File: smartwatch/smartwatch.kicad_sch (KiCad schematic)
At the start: 33 parts, among them J1 BAT_CON, J2 DC_CON, J3 PROG_INT, J4 Screen, J5 Touch, J6 Power, J8 SD Card, SW1 SW_Push, U1 ESP32-WROVER-E, U2 MCP73831-5-OT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

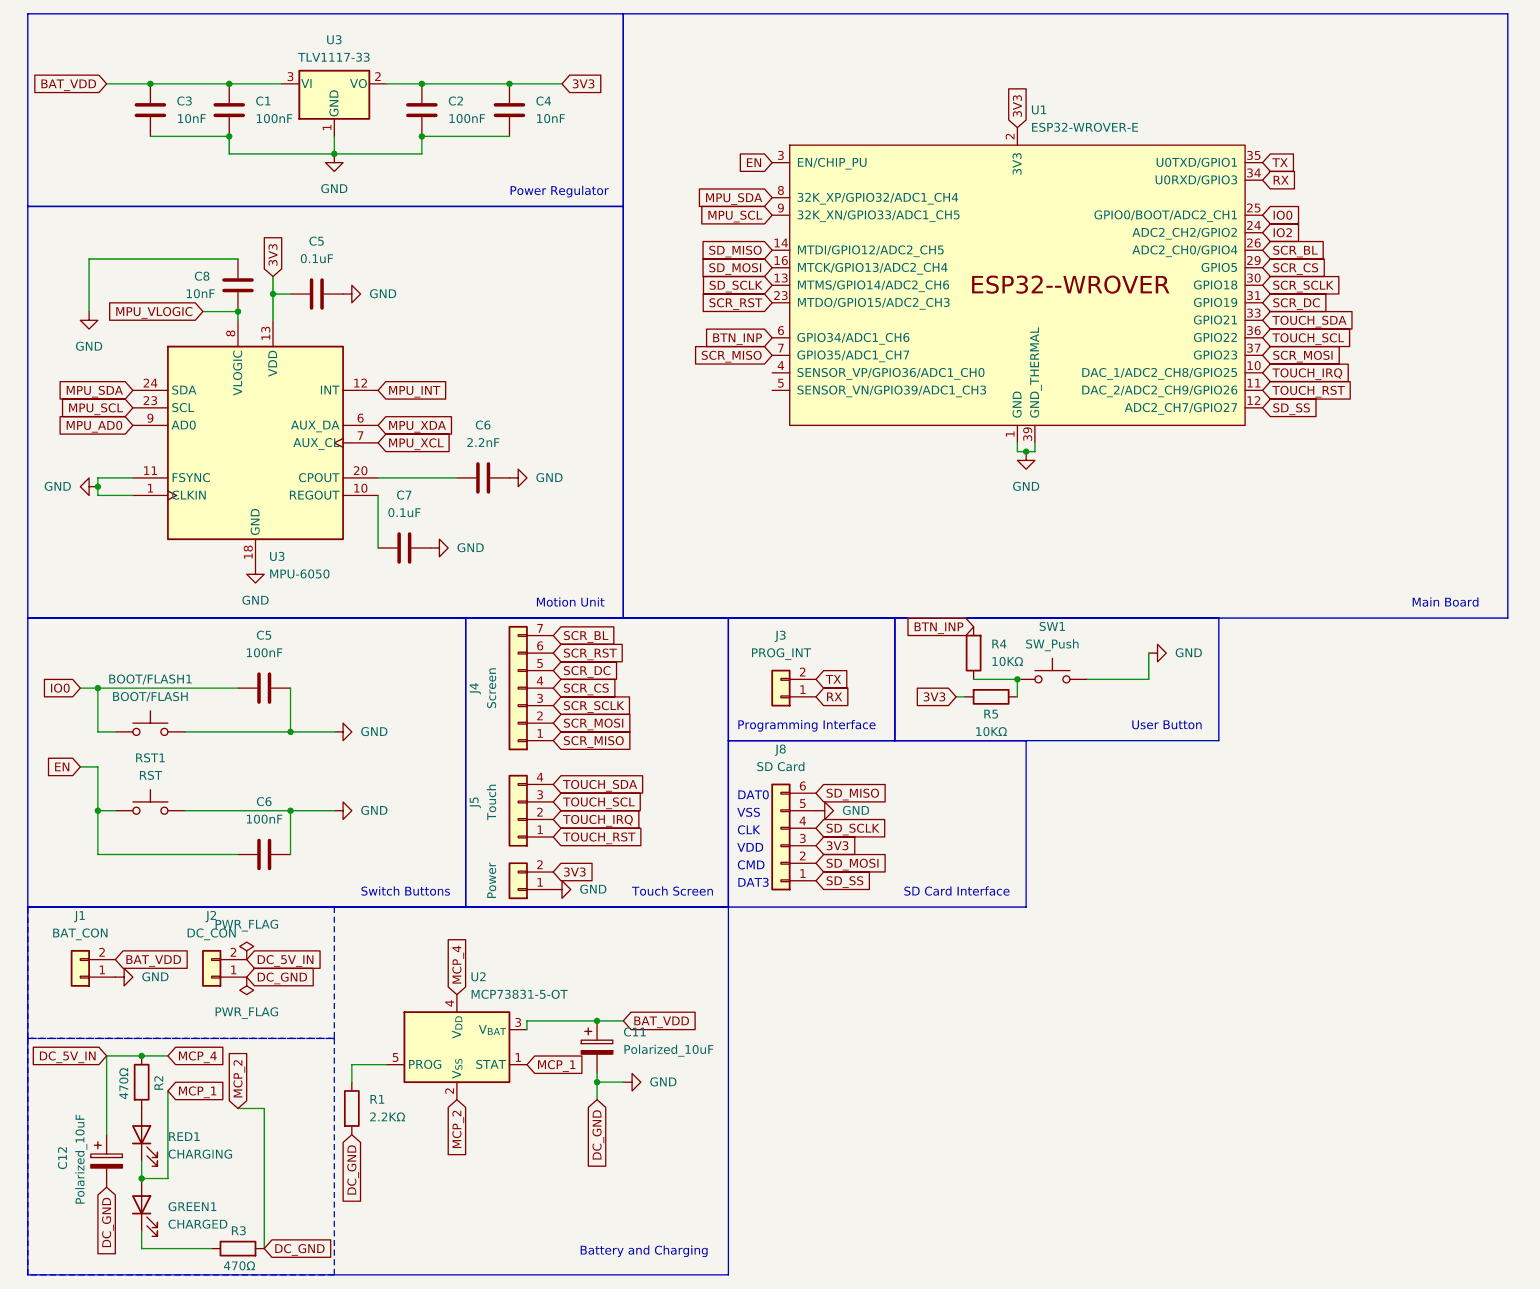
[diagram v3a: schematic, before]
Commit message: fully redesigned board - ground and power planes :)
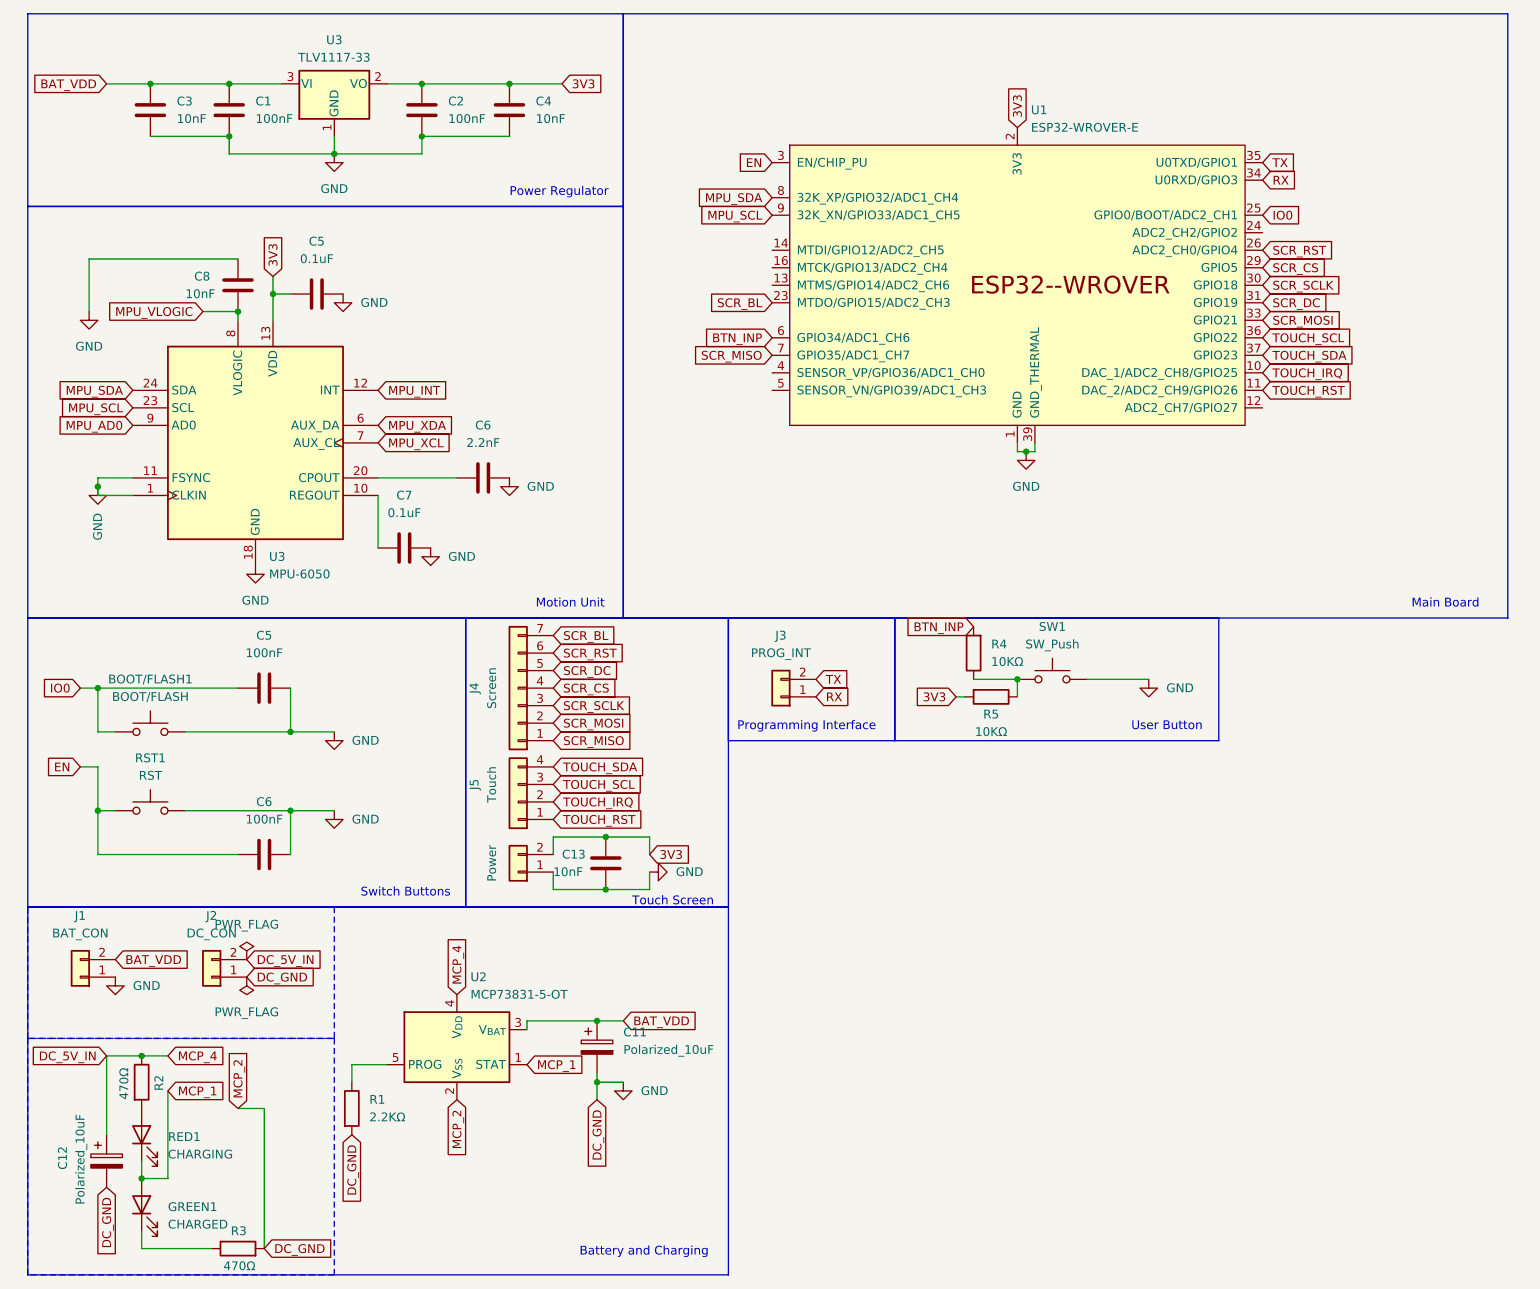
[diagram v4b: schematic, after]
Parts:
- removed J8: SD Card, Connector_Wire_SMD:Wire_Pad_1x06, symbol Connector_Generic:Conn_01x06
- added C13: 10nF, Capacitor_SMD:C_0805_2012Metric_Pad1.18x1.45mm_HandSolder, symbol Device:C
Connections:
- net 3V3: now also C13.2
- net GND: now also C13.1
- net SCR_BL: now also U1.23 (MTDO/GPIO15/ADC2_CH3); no longer U1.26 (ADC2_CH0/GPIO4)
- net SCR_MOSI: now also U1.33 (GPIO21); no longer U1.37 (GPIO23)
- net SCR_RST: now also U1.26 (ADC2_CH0/GPIO4); no longer U1.23 (MTDO/GPIO15/ADC2_CH3)
- net TOUCH_SDA: now also U1.37 (GPIO23); no longer U1.33 (GPIO21)
- net IO2: no longer names the net of U1.24 (ADC2_CH2/GPIO2)
- net SD_MISO: no longer names the net of U1.14 (MTDI/GPIO12/ADC2_CH5)
- net SD_MOSI: no longer names the net of U1.16 (MTCK/GPIO13/ADC2_CH4)
- net SD_SCLK: no longer names the net of U1.13 (MTMS/GPIO14/ADC2_CH6)
- net SD_SS: no longer names the net of U1.12 (ADC2_CH7/GPIO27)
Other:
- note removed: "CLK"
- note removed: "CMD"
- note removed: "DAT0"
- note removed: "DAT3"
- note removed: "SD Card Interface"
- note removed: "VDD"
- note removed: "VSS"
- moved on the sheet: J5

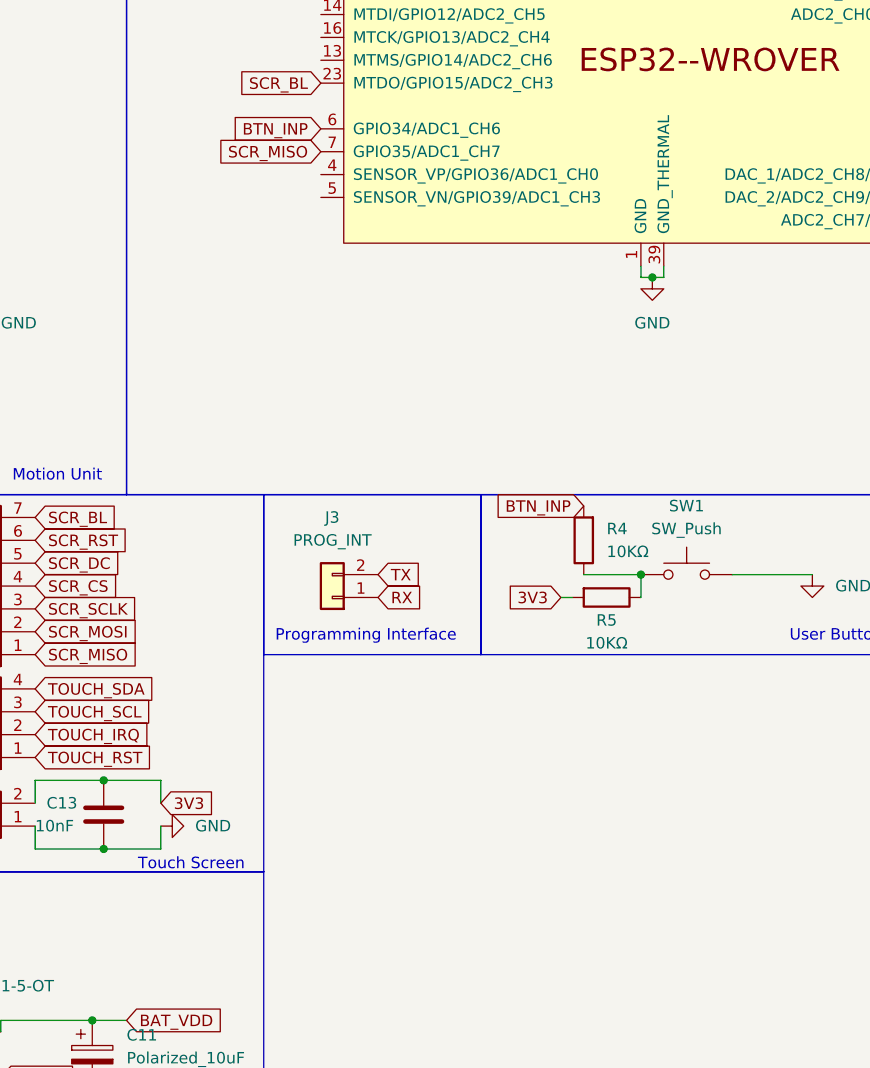
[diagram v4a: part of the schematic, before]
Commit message: implemented battery reading in both code and schem
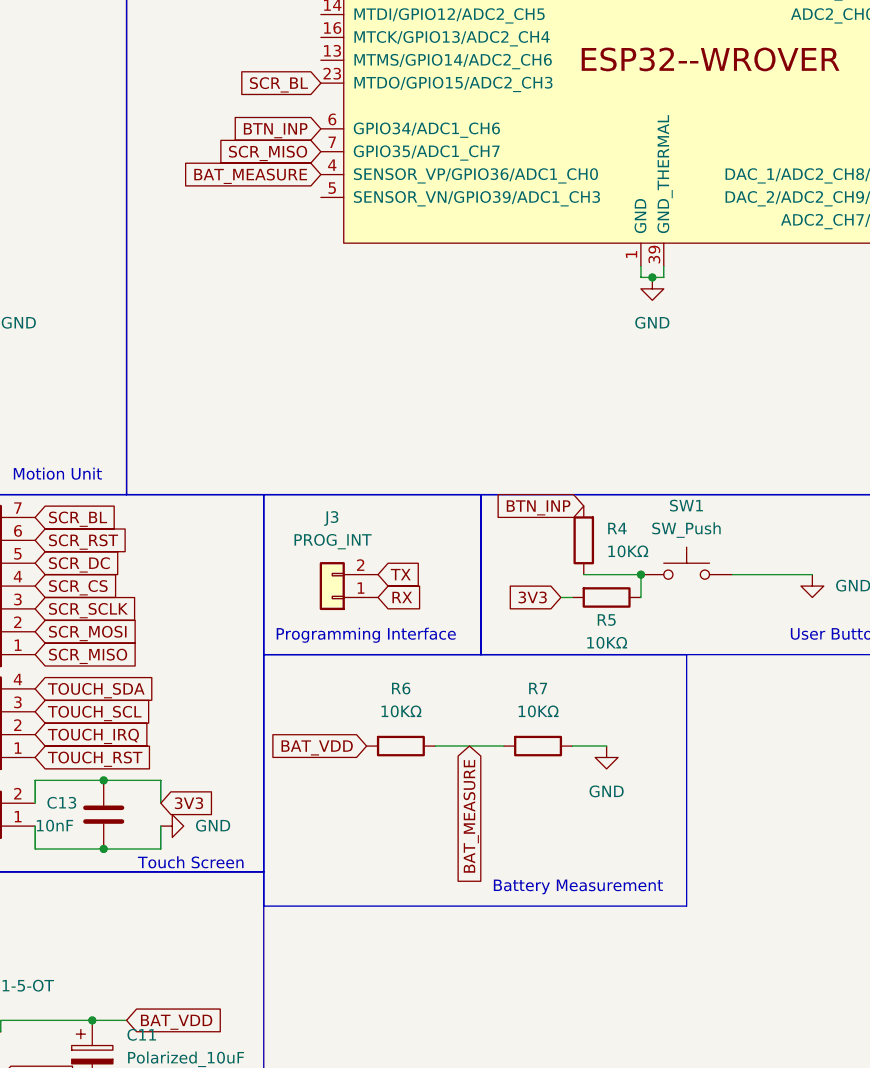
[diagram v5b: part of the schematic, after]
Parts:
- added R6, R7: 10KΩ, Resistor_SMD:R_0805_2012Metric_Pad1.20x1.40mm_HandSolder, symbol Device:R
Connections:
- net BAT_VDD: now also R6.2
- net GND: now also R7.1
- net BAT_MEASURE: now reaches U1.4 (SENSOR_VP/GPIO36/ADC1_CH0)
- net BAT_MEASURE: now also R6.1, R7.2
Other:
- note added: "Battery Measurement"
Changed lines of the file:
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@@
+    (stroke (width 0) (type default))
+  )
+  (wire (pts (xy 135.89 129.54) (xy 143.51 129.54))
     (stroke (width 0) (type default))
   )
@@
     (stroke (width 0) (type default))
   )
+  (wire (pts (xy 151.13 129.54) (xy 154.94 129.54))
+    (stroke (width 0) (type default))
+  )
   (wire (pts (xy 91.44 140.97) (xy 99.06 140.97))
     (stroke (width 0) (type default))
@@
   (wire (pts (xy 45.72 135.89) (xy 25.4 135.89))
     (stroke (width 0) (type default))
+  )
+  (rectangle (start 116.84 119.38) (end 163.83 147.32)
+    (stroke (width 0) (type default))
+    (fill (type none))
   )
   (rectangle (start 15.24 13.97) (end 101.6 41.91)
@@
     (fill (type none))
   )
+  (text "Battery Measurement" (at 142.24 146.05 0)
+    (effects (font (size 1.27 1.27)) (justify left bottom))
+  )
   (text "User Button" (at 175.26 118.11 0)
     (effects (font (size 1.27 1.27)) (justify left bottom))
@@
     )
   )
+  (global_label "BAT_MEASURE" (shape input) (at 139.7 129.54 270) (fields_autoplaced)
+    (effects (font (size 1.27 1.27)) (justify right))
+    (property "Intersheetrefs" "${INTERSHEET_REFS}" (at 139.7 145.3876 90)
+      (effects (font (size 1.27 1.27)) (justify right) hide)
+    )
+  )
   (global_label "MCP_1" (shape input) (at 87.63 166.37 0) (fields_autoplaced)
     (effects (font (size 1.27 1.27)) (justify left))
@@
     )
   )
+  (global_label "BAT_MEASURE" (shape input) (at 123.19 66.04 180) (fields_autoplaced)
+    (effects (font (size 1.27 1.27)) (justify right))
+    (property "Intersheetrefs" "${INTERSHEET_REFS}" (at 107.3424 66.04 0)
+      (effects (font (size 1.27 1.27)) (justify right) hide)
+    )
+  )
   (global_label "MCP_4" (shape input) (at 35.56 165.1 0) (fields_autoplaced)
     (effects (font (size 1.27 1.27)) (justify left))
@@
     )
   )
+  (global_label "BAT_VDD" (shape input) (at 128.27 129.54 180) (fields_autoplaced)
+    (effects (font (size 1.27 1.27)) (justify right))
+    (property "Intersheetrefs" "${INTERSHEET_REFS}" (at 117.4418 129.54 0)
+      (effects (font (size 1.27 1.27)) (justify right) hide)
+    )
+  )
   (global_label "MPU_SDA" (shape input) (at 30.48 68.58 180) (fields_autoplaced)
     (effects (font (size 1.27 1.27)) (justify right))
@@
     (property "Intersheetrefs" "${INTERSHEET_REFS}" (at 18.9866 73.66 0)
       (effects (font (size 1.27 1.27)) (justify right) hide)
+    )
+  )
+  (symbol (lib_id "Device:R") (at 147.32 129.54 270) (unit 1)
+    (in_bom yes) (on_board yes) (dnp no) (fields_autoplaced)
+    (property "Reference" "R7" (at 147.32 123.19 90)
+      (effects (font (size 1.27 1.27)))
+    )
+    (property "Value" "10KΩ" (at 147.32 125.73 90)
+      (effects (font (size 1.27 1.27)))
+    )
+    (property "Footprint" "Resistor_SMD:R_0805_2012Metric_Pad1.20x1.40mm_HandSolder" (at 147.32 127.762 90)
+      (effects (font (size 1.27 1.27)) hide)
+    )
+    (property "Datasheet" "~" (at 147.32 129.54 0)
+      (effects (font (size 1.27 1.27)) hide)
+    )
+    (pin "1")
+    (pin "2")
+    (instances
+      (project "smartwatch"
+        (path "/ed763a40-a5bc-4ad5-80fd-af92dd7e1451"
+          (reference "R7") (unit 1)
+        )
+      )
     )
   )
@@
         (path "/ed763a40-a5bc-4ad5-80fd-af92dd7e1451"
           (reference "#PWR09") (unit 1)
+        )
+      )
+    )
+  )
+  (symbol (lib_id "Device:R") (at 132.08 129.54 270) (unit 1)
+    (in_bom yes) (on_board yes) (dnp no) (fields_autoplaced)
+    (property "Reference" "R6" (at 132.08 123.19 90)
+      (effects (font (size 1.27 1.27)))
+    )
+    (property "Value" "10KΩ" (at 132.08 125.73 90)
+      (effects (font (size 1.27 1.27)))
+    )
+    (property "Footprint" "Resistor_SMD:R_0805_2012Metric_Pad1.20x1.40mm_HandSolder" (at 132.08 127.762 90)
+      (effects (font (size 1.27 1.27)) hide)
+    )
+    (property "Datasheet" "~" (at 132.08 129.54 0)
+      (effects (font (size 1.27 1.27)) hide)
+    )
+    (pin "1")
+    (pin "2")
+    (instances
+      (project "smartwatch"
+        (path "/ed763a40-a5bc-4ad5-80fd-af92dd7e1451"
+          (reference "R6") (unit 1)
         )
       )
@@
         )
       )
+    )
+  )
+  (symbol (lib_id "power:GND") (at 154.94 129.54 0) (unit 1)
+    (in_bom yes) (on_board yes) (dnp no) (fields_autoplaced)
+    (property "Reference" "#PWR015" (at 154.94 135.89 0)
+      (effects (font (size 1.27 1.27)) hide)
+    )
+    (property "Value" "GND" (at 154.94 134.62 0)
+      (effects (font (size 1.27 1.27)))
+    )
+    (property "Footprint" "" (at 154.94 129.54 0)
+      (effects (font (size 1.27 1.27)) hide)
+    )
+    (property "Datasheet" "" (at 154.94 129.54 0)
+      (effects (font (size 1.27 1.27)) hide)
+    )
+    (pin "1")
+    (instances
+      (project "smartwatch"
+        (path "/ed763a40-a5bc-4ad5-80fd-af92dd7e1451"
+          (reference "#PWR015") (unit 1)
+        )
+      )

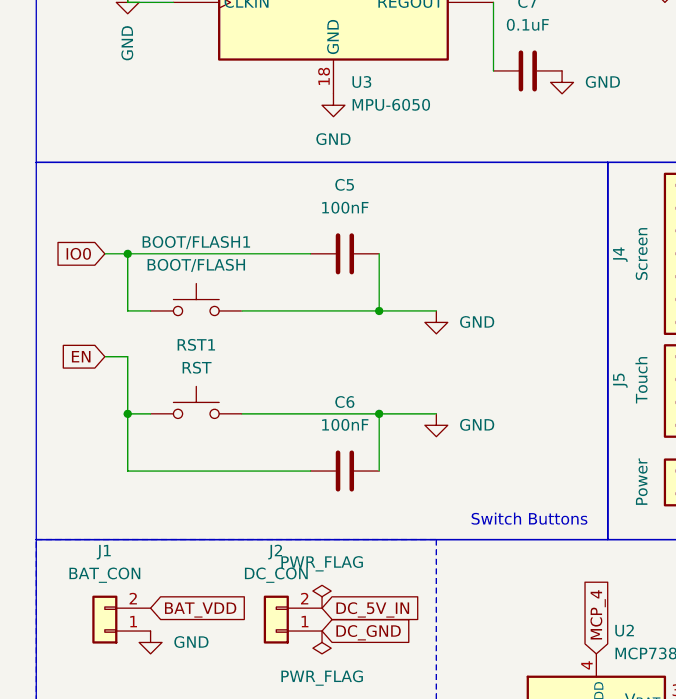
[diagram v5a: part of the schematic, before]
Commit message: added missing pullups
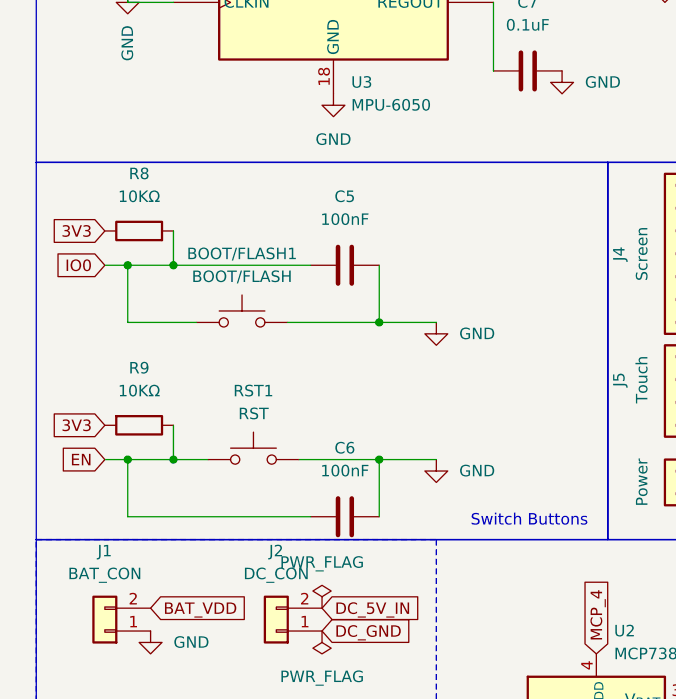
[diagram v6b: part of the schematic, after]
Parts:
- added R8, R9: 10KΩ, Resistor_SMD:R_0805_2012Metric_Pad1.20x1.40mm_HandSolder, symbol Device:R
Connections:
- net 3V3: now also R8.1, R9.2
- net EN: now also R9.1
- net IO0: now also R8.2
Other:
- moved on the sheet: BOOT/FLASH1, C5, C6, RST1

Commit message: added connector
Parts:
- removed J4: Screen, Connector_Wire_SMD:Wire_Pad_1x07, symbol Connector_Generic:Conn_01x07
- removed J5: Touch, Connector_Wire_SMD:Wire_Pad_1x04, symbol Connector_Generic:Conn_01x04
- removed J6: Power, Connector_Wire_SMD:Wire_Pad_1x02, symbol Connector_Generic:Conn_01x02
- added J4: SM13B-GHS-TB, SM13B-GHS-TB:JST_SM13B-GHS-TB, symbol SM13B-GHS-TB:SM13B-GHS-TB
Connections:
- net 3V3: now also C13.1, J4.1; no longer C13.2
- net BAT_MEASURE: now also R6.2, R7.1; no longer R6.1, R7.2
- net BAT_VDD: now also R6.1; no longer R6.2
- net GND: now also C13.2, R7.2, J4.2, J4.SH1 (SHIELD), J4.SH2 (SHIELD); no longer C13.1, R7.1
- net SCR_BL: now also J4.9
- net SCR_CS: now also J4.6
- net SCR_DC: now also J4.7
- net SCR_MISO: now also J4.3
- net SCR_MOSI: now also J4.4
- net SCR_RST: now also J4.8
- net SCR_SCLK: now also J4.5
- net TOUCH_IRQ: now also J4.12
- net TOUCH_RST: now also J4.13
- net TOUCH_SCL: now also J4.11
- net TOUCH_SDA: now also J4.10
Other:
- note added: "Screen Connector"
- note removed: "Touch Screen"
- moved on the sheet: R6, R7
